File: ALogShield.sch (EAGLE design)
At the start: 29 parts, among them U1 DS3231MZ/V+T

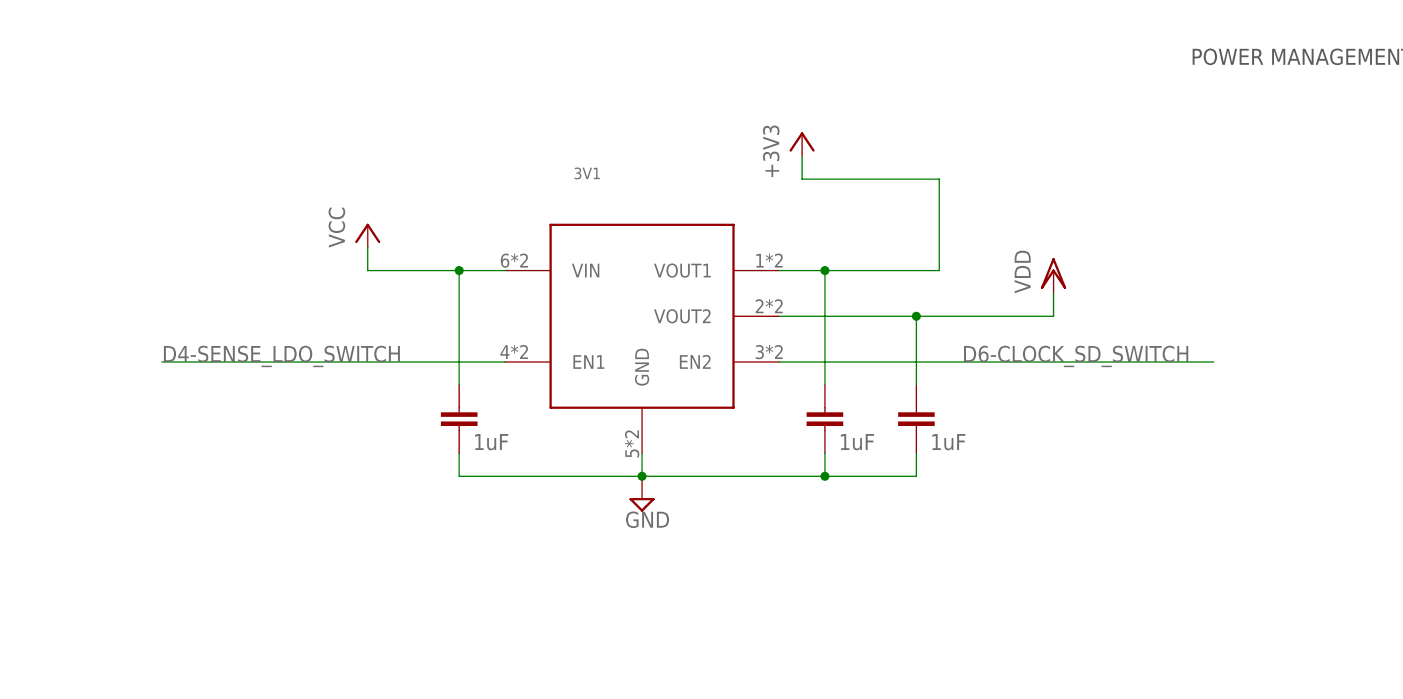
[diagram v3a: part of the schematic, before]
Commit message: Remove 3V3; connect 3V3 and VDD
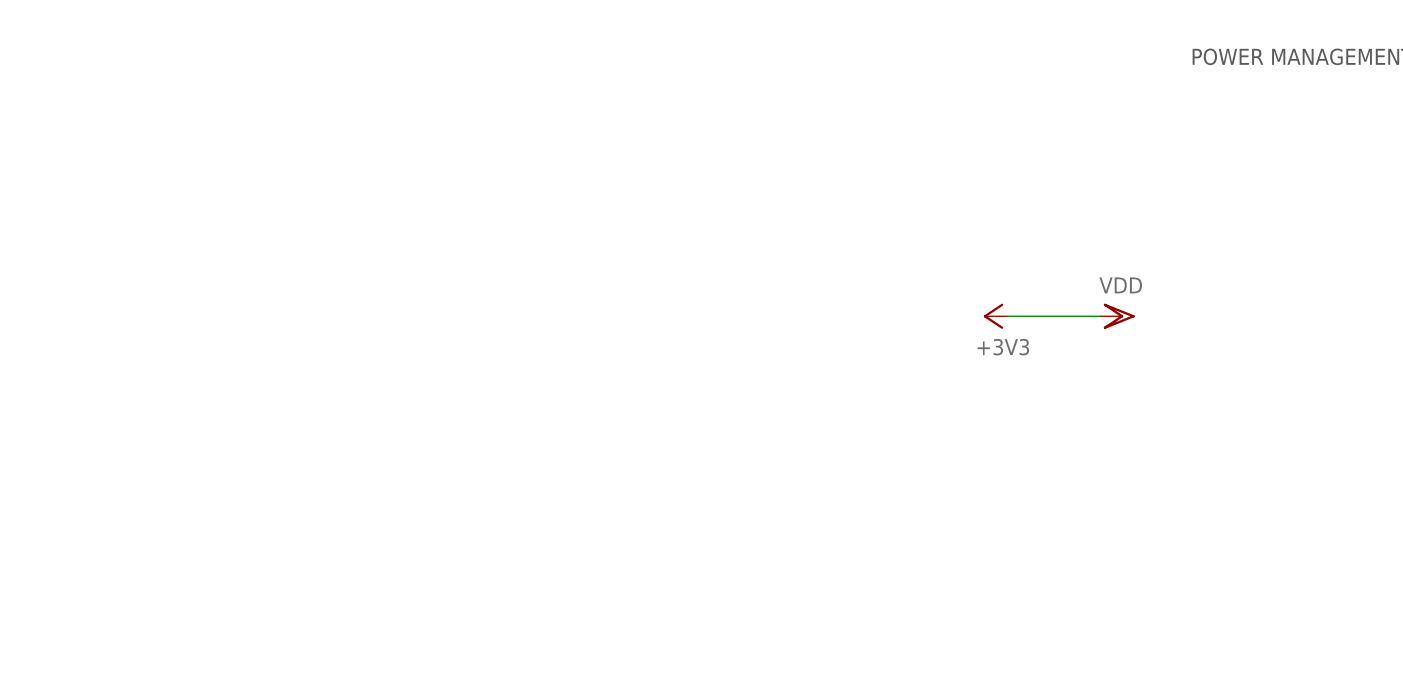
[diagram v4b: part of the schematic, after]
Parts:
- removed 3V1: MIC5380_LARGE_PADS, csandell:MIC5380_LARGE_PADS
- removed CLOCK_CIN1, CLOCK_CIN2, CLOCK_CIN3: 1uF, rcl:C-EUC0603
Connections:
- net +3V3: no longer 3V1.VOUT1, CLOCK_CIN2.1
- net D4-SENSE_LDO_SWITCH: no longer 3V1.EN1
- net D6-CLOCK_SD_SWITCH: no longer 3V1.EN2
- net GND: no longer 3V1.GND, CLOCK_CIN1.2, CLOCK_CIN2.2, CLOCK_CIN3.2
- net VCC: no longer 3V1.VIN, CLOCK_CIN1.1
- net VDD: no longer 3V1.VOUT2, CLOCK_CIN3.1
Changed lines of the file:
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@@
 <part name="FRAME4" library="frames" deviceset="LETTER_P" device=""/>
 <part name="FRAME5" library="frames" deviceset="LETTER_P" device=""/>
-<part name="CLOCK_CIN1" library="rcl" deviceset="C-EU" device="C0603" value="1uF"/>
-<part name="CLOCK_CIN2" library="rcl" deviceset="C-EU" device="C0603" value="1uF"/>
-<part name="CLOCK_CIN3" library="rcl" deviceset="C-EU" device="C0603" value="1uF"/>
-<part name="SUPPLY72" library="supply2" deviceset="GND" device=""/>
 <part name="+3V15" library="supply1" deviceset="+3V3" device=""/>
-<part name="P+22" library="supply1" deviceset="VCC" device=""/>
 <part name="SD_3V4" library="supply1" deviceset="VDD" device=""/>
 <part name="SD_3V5" library="supply1" deviceset="VDD" device=""/>
@@
 <part name="J2" library="SparkFun-Connectors" deviceset="CONN_04" device="SCREW"/>
 <part name="I2C_PU_" library="resistor-dil" deviceset="4R-N" device="0603-ARC" value="3.3K"/>
-<part name="3V1" library="csandell" deviceset="MIC5380_LARGE_PADS" device=""/>
 <part name="C15" library="rc-master-smd" deviceset="CCA_" device="" value="10nF"/>
 <part name="CLOCK_BATT" library="awickert" deviceset="LINX-BAT-HLD-012-SMT-OTL" device="" value="Linx BAT-HLD-012-SMT"/>
@@
 <attribute name="DRAWING_NAME" x="294.64" y="-486.41" size="2.54" layer="94"/>
 </instance>
-<instance part="CLOCK_CIN1" gate="G$1" x="241.3" y="-48.26" smashed="yes">
-<attribute name="VALUE" x="242.824" y="-52.959" size="1.778" layer="96"/>
-</instance>
-<instance part="CLOCK_CIN2" gate="G$1" x="281.94" y="-48.26" smashed="yes">
-<attribute name="VALUE" x="283.464" y="-52.959" size="1.778" layer="96"/>
-</instance>
-<instance part="CLOCK_CIN3" gate="G$1" x="292.1" y="-48.26" smashed="yes">
-<attribute name="VALUE" x="293.624" y="-52.959" size="1.778" layer="96"/>
-</instance>
-<instance part="SUPPLY72" gate="GND" x="261.62" y="-58.42"/>
-<instance part="+3V15" gate="G$1" x="279.4" y="-17.78"/>
-<instance part="P+22" gate="VCC" x="231.14" y="-27.94"/>
-<instance part="SD_3V4" gate="G$1" x="307.34" y="-33.02"/>
+<instance part="+3V15" gate="G$1" x="299.72" y="-38.1" rot="R90"/>
+<instance part="SD_3V4" gate="G$1" x="314.96" y="-38.1" rot="R270"/>
 <instance part="SD_3V5" gate="G$1" x="254" y="-289.56"/>
 <instance part="SD_3V6" gate="G$1" x="307.34" y="-276.86"/>
@@
 <attribute name="NAME" x="127.508" y="-403.86" size="1.778" layer="95" rot="R90"/>
 </instance>
-<instance part="3V1" gate="G$1" x="261.62" y="-38.1"/>
 <instance part="C15" gate="A" x="48.26" y="-195.58"/>
 <instance part="C15" gate="B" x="48.26" y="-185.42"/>
@@
 <pinref part="P+3" gate="VCC" pin="VCC"/>
 <pinref part="H4" gate="G$1" pin="5"/>
-</segment>
-<segment>
-<wire x1="246.38" y1="-33.02" x2="241.3" y2="-33.02" width="0.1524" layer="91"/>
-<wire x1="241.3" y1="-33.02" x2="231.14" y2="-33.02" width="0.1524" layer="91"/>
-<wire x1="241.3" y1="-33.02" x2="241.3" y2="-45.72" width="0.1524" layer="91"/>
-<pinref part="CLOCK_CIN1" gate="G$1" pin="1"/>
-<junction x="241.3" y="-33.02"/>
-<pinref part="P+22" gate="VCC" pin="VCC"/>
-<wire x1="231.14" y1="-33.02" x2="231.14" y2="-30.48" width="0.1524" layer="91"/>
-<pinref part="3V1" gate="G$1" pin="VIN"/>
 </segment>
 <segment>
@@
 </segment>
 <segment>
-<wire x1="261.62" y1="-53.34" x2="261.62" y2="-55.88" width="0.1524" layer="91"/>
-<wire x1="261.62" y1="-55.88" x2="281.94" y2="-55.88" width="0.1524" layer="91"/>
-<wire x1="281.94" y1="-55.88" x2="292.1" y2="-55.88" width="0.1524" layer="91"/>
-<wire x1="261.62" y1="-55.88" x2="241.3" y2="-55.88" width="0.1524" layer="91"/>
-<pinref part="SUPPLY72" gate="GND" pin="GND"/>
-<junction x="261.62" y="-55.88"/>
-<pinref part="CLOCK_CIN3" gate="G$1" pin="2"/>
-<wire x1="292.1" y1="-53.34" x2="292.1" y2="-55.88" width="0.1524" layer="91"/>
-<pinref part="CLOCK_CIN2" gate="G$1" pin="2"/>
-<wire x1="281.94" y1="-53.34" x2="281.94" y2="-55.88" width="0.1524" layer="91"/>
-<pinref part="CLOCK_CIN1" gate="G$1" pin="2"/>
-<wire x1="241.3" y1="-53.34" x2="241.3" y2="-55.88" width="0.1524" layer="91"/>
-<junction x="281.94" y="-55.88"/>
-<pinref part="3V1" gate="G$1" pin="GND"/>
-</segment>
-<segment>
 <pinref part="J1" gate="G$1" pin="2"/>
 <pinref part="SUPPLY1" gate="GND" pin="GND"/>
@@
 </segment>
 <segment>
-<pinref part="+3V15" gate="G$1" pin="+3V3"/>
-<wire x1="279.4" y1="-20.32" x2="279.4" y2="-22.86" width="0.1524" layer="91"/>
-<wire x1="276.86" y1="-33.02" x2="281.94" y2="-33.02" width="0.1524" layer="91"/>
-<pinref part="CLOCK_CIN2" gate="G$1" pin="1"/>
-<wire x1="281.94" y1="-33.02" x2="294.64" y2="-33.02" width="0.1524" layer="91"/>
-<wire x1="281.94" y1="-45.72" x2="281.94" y2="-33.02" width="0.1524" layer="91"/>
-<junction x="281.94" y="-33.02"/>
-<wire x1="294.64" y1="-33.02" x2="294.64" y2="-22.86" width="0.1524" layer="91"/>
-<wire x1="294.64" y1="-22.86" x2="279.4" y2="-22.86" width="0.1524" layer="91"/>
-<pinref part="3V1" gate="G$1" pin="VOUT1"/>
-</segment>
-<segment>
 <wire x1="50.8" y1="-132.08" x2="20.32" y2="-132.08" width="0.1524" layer="91"/>
 <pinref part="+3V16" gate="G$1" pin="+3V3"/>
@@
 <pinref part="H4" gate="G$1" pin="8"/>
 <pinref part="+3V1" gate="G$1" pin="+3V3"/>
+</segment>
+<segment>
+<pinref part="SD_3V4" gate="G$1" pin="VDD"/>
+<wire x1="302.26" y1="-38.1" x2="312.42" y2="-38.1" width="0.1524" layer="91"/>
+<pinref part="+3V15" gate="G$1" pin="+3V3"/>
 </segment>
 </net>
@@
 <net name="VDD" class="0">
 <segment>
-<wire x1="276.86" y1="-38.1" x2="292.1" y2="-38.1" width="0.1524" layer="91"/>
-<pinref part="CLOCK_CIN3" gate="G$1" pin="1"/>
-<wire x1="292.1" y1="-45.72" x2="292.1" y2="-38.1" width="0.1524" layer="91"/>
-<wire x1="292.1" y1="-38.1" x2="307.34" y2="-38.1" width="0.1524" layer="91"/>
-<pinref part="SD_3V4" gate="G$1" pin="VDD"/>
-<wire x1="307.34" y1="-38.1" x2="307.34" y2="-35.56" width="0.1524" layer="91"/>
-<junction x="292.1" y="-38.1"/>
-<pinref part="3V1" gate="G$1" pin="VOUT2"/>
-</segment>
-<segment>
 <wire x1="254" y1="-294.64" x2="259.08" y2="-294.64" width="0.1524" layer="91"/>
 <pinref part="SD1" gate="G$1" pin="VDD"/>
@@
 <net name="D4-SENSE_LDO_SWITCH" class="0">
 <segment>
-<wire x1="246.38" y1="-43.18" x2="208.28" y2="-43.18" width="0.1524" layer="91"/>
-<label x="208.28" y="-43.18" size="1.778" layer="95"/>
-<pinref part="3V1" gate="G$1" pin="EN1"/>
-</segment>
-<segment>
 <wire x1="53.34" y1="-45.72" x2="63.5" y2="-45.72" width="0.1524" layer="91"/>
 <pinref part="U$9" gate="G$1" pin="D4"/>
@@
 <net name="D6-CLOCK_SD_SWITCH" class="0">
 <segment>
-<wire x1="276.86" y1="-43.18" x2="325.12" y2="-43.18" width="0.1524" layer="91"/>
-<label x="297.18" y="-43.18" size="1.778" layer="95"/>
-<pinref part="3V1" gate="G$1" pin="EN2"/>
-</segment>
-<segment>
 <wire x1="53.34" y1="-50.8" x2="63.5" y2="-50.8" width="0.1524" layer="91"/>

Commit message: IOREF to VCC
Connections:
- net GND: no longer U$9.IOREF
- net VCC: now also U$9.IOREF
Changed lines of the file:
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@@
 <wire x1="162.56" y1="-66.04" x2="162.56" y2="-55.88" width="0.1524" layer="91"/>
 <pinref part="P+8" gate="VCC" pin="VCC"/>
+<wire x1="124.46" y1="-66.04" x2="137.16" y2="-66.04" width="0.1524" layer="91"/>
+<pinref part="U$9" gate="G$1" pin="IOREF"/>
+<label x="129.54" y="-66.04" size="1.778" layer="95"/>
+<wire x1="137.16" y1="-66.04" x2="137.16" y2="-71.12" width="0.1524" layer="91"/>
+<wire x1="137.16" y1="-71.12" x2="154.94" y2="-71.12" width="0.1524" layer="91"/>
+<wire x1="154.94" y1="-71.12" x2="154.94" y2="-66.04" width="0.1524" layer="91"/>
+<junction x="154.94" y="-66.04"/>
 </segment>
 <segment>
@@
 </segment>
 <segment>
+<pinref part="SUPPLY40" gate="GND" pin="GND"/>
 <wire x1="124.46" y1="-68.58" x2="134.62" y2="-68.58" width="0.1524" layer="91"/>
 <pinref part="U$9" gate="G$1" pin="NC"/>
-<pinref part="SUPPLY40" gate="GND" pin="GND"/>
-<wire x1="124.46" y1="-66.04" x2="134.62" y2="-66.04" width="0.1524" layer="91"/>
-<pinref part="U$9" gate="G$1" pin="IOREF"/>
-<label x="129.54" y="-66.04" size="1.778" layer="95"/>
-<wire x1="134.62" y1="-66.04" x2="134.62" y2="-68.58" width="0.1524" layer="91"/>
-<junction x="134.62" y="-68.58"/>
 </segment>
 <segment>
